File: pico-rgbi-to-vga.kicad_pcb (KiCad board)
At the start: 2 copper layers, 68.8 x 59 mm, 25 parts, among them J1 SDS-80J, J2 DB15_Female_HighDensity, J3 USB-B1HSB6, SW1 SW_Push, SW2 Intensity Select, U1 Pico

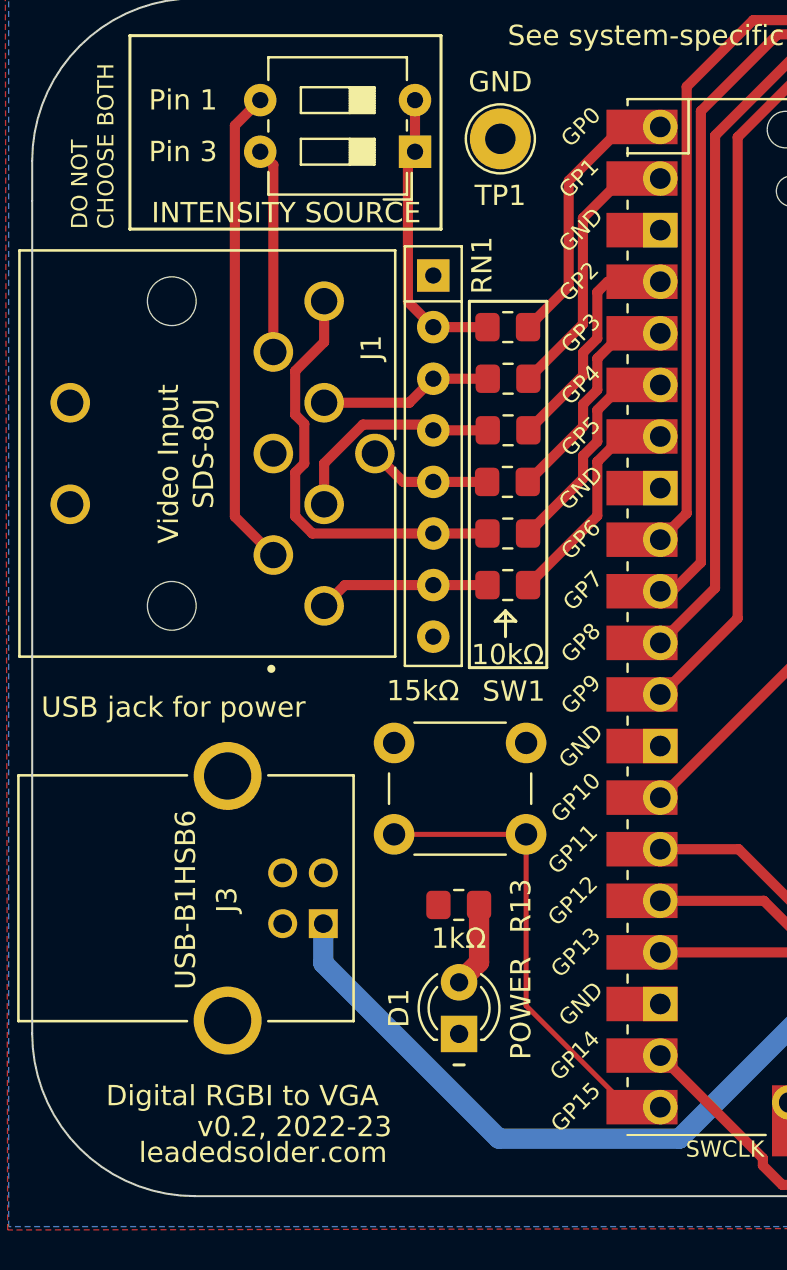
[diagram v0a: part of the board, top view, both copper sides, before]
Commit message: Fix boneheaded pinout mixup
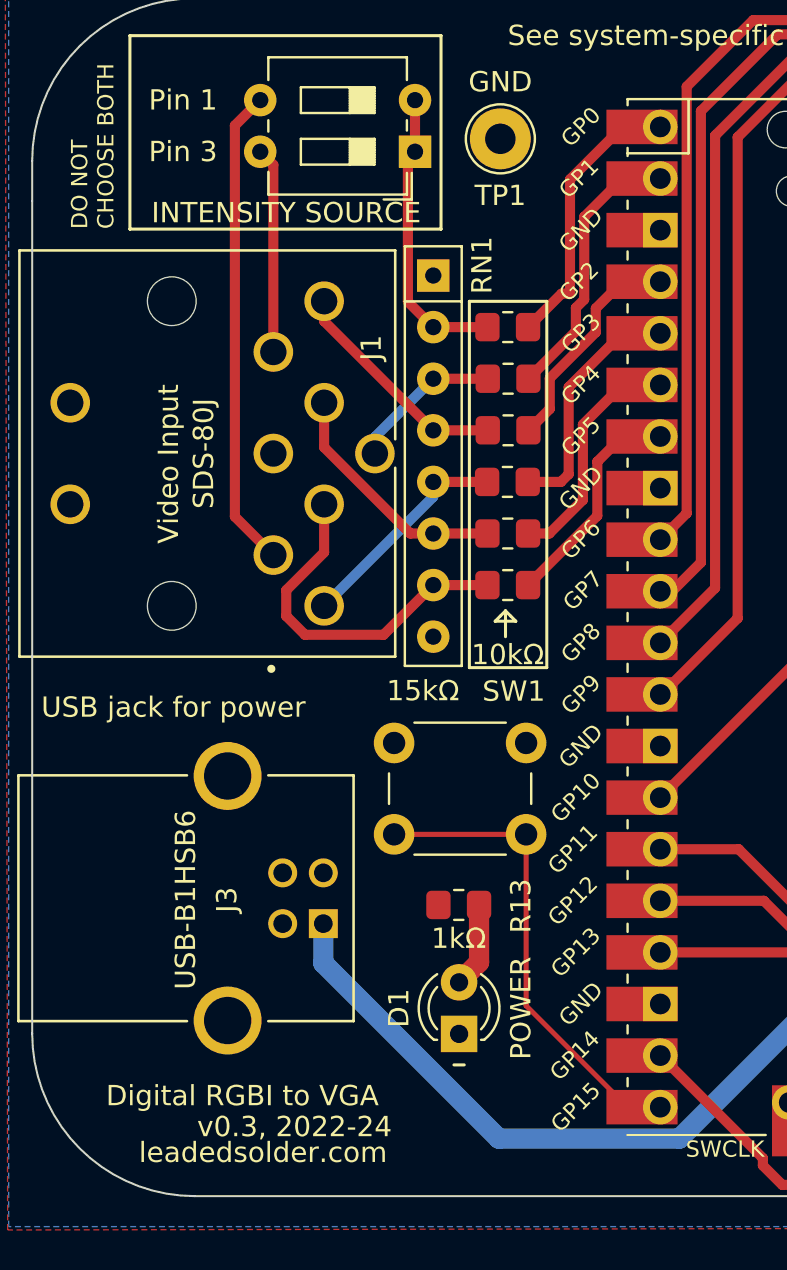
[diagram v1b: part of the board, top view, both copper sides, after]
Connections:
- R1 pad 2: /RED_IN -> /HSYNC_IN
- R2 pad 2: /GREEN_IN -> /VSYNC_IN
- R3 pad 2: /BLUE_IN -> /RED_IN
- R4 pad 2: /HSYNC_IN -> /GREEN_IN
- R5 pad 2: /VSYNC_IN -> /BLUE_IN
- RN1 pad 3: /VSYNC_IN -> /BLUE_IN
- RN1 pad 4: /HSYNC_IN -> /GREEN_IN
- RN1 pad 5: /BLUE_IN -> /RED_IN
- RN1 pad 6: /GREEN_IN -> /VSYNC_IN
- RN1 pad 7: /RED_IN -> /HSYNC_IN
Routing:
- net /GREEN_IN: track 21.4 -> 11.3 mm
- net /HSYNC_IN: track 11.0 -> 17.6 mm
- net /VSYNC_IN: track 8.55 -> 12.0 mm
- net /RED_IN: track 8.46 -> 11.0 mm
- net /BLUE_IN: track 6.10 -> 7.56 mm
- net /RED_3v3: track 11.1 -> 12.1 mm
- net /VSYNC_3v3: track 11.1 -> 11.7 mm
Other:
- board text added: "B"
- board text added: "G"
- board text added: "Hs"
- board text added: "I"
- board text added: "R"
- board text added: "Vs"
- board text added: "v0.3, 2022-24"
- board text removed: "v0.2, 2022-23"

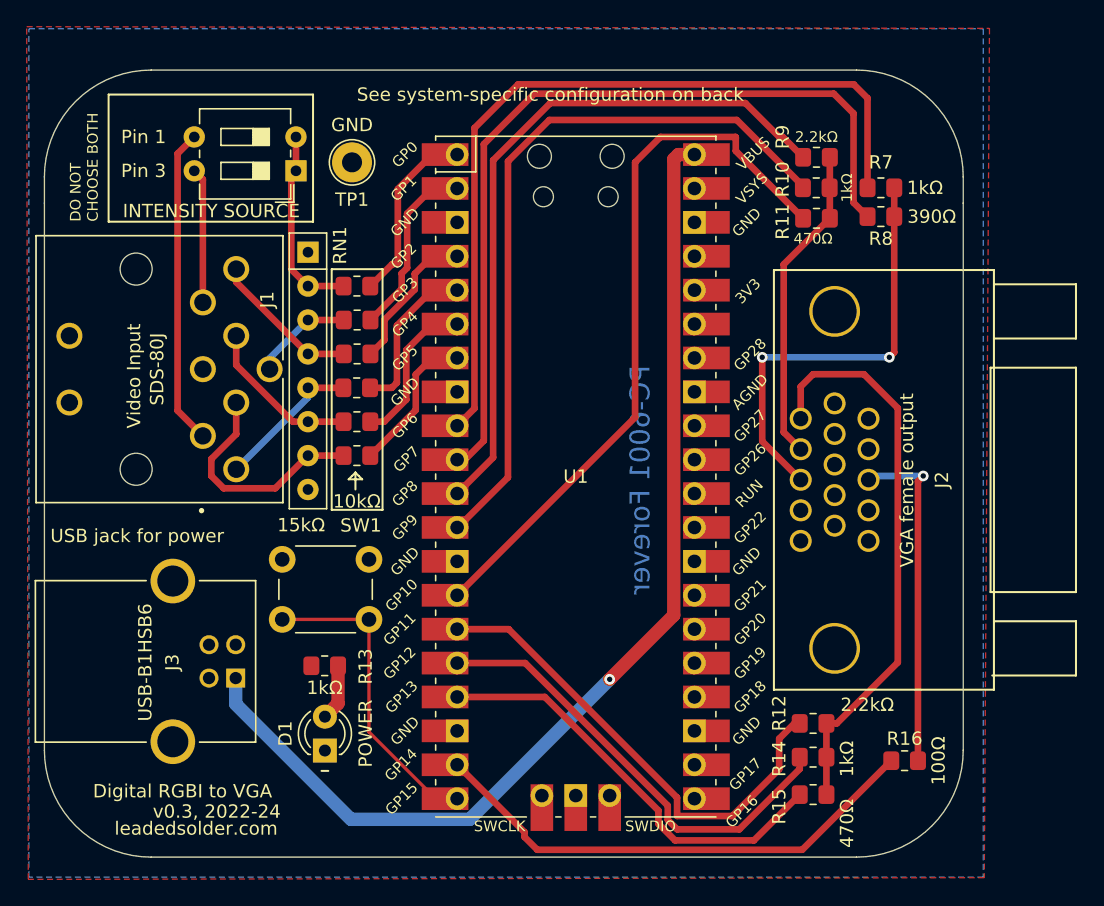
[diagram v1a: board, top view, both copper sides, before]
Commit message: V0.3 prep, adding logic analyzer lines
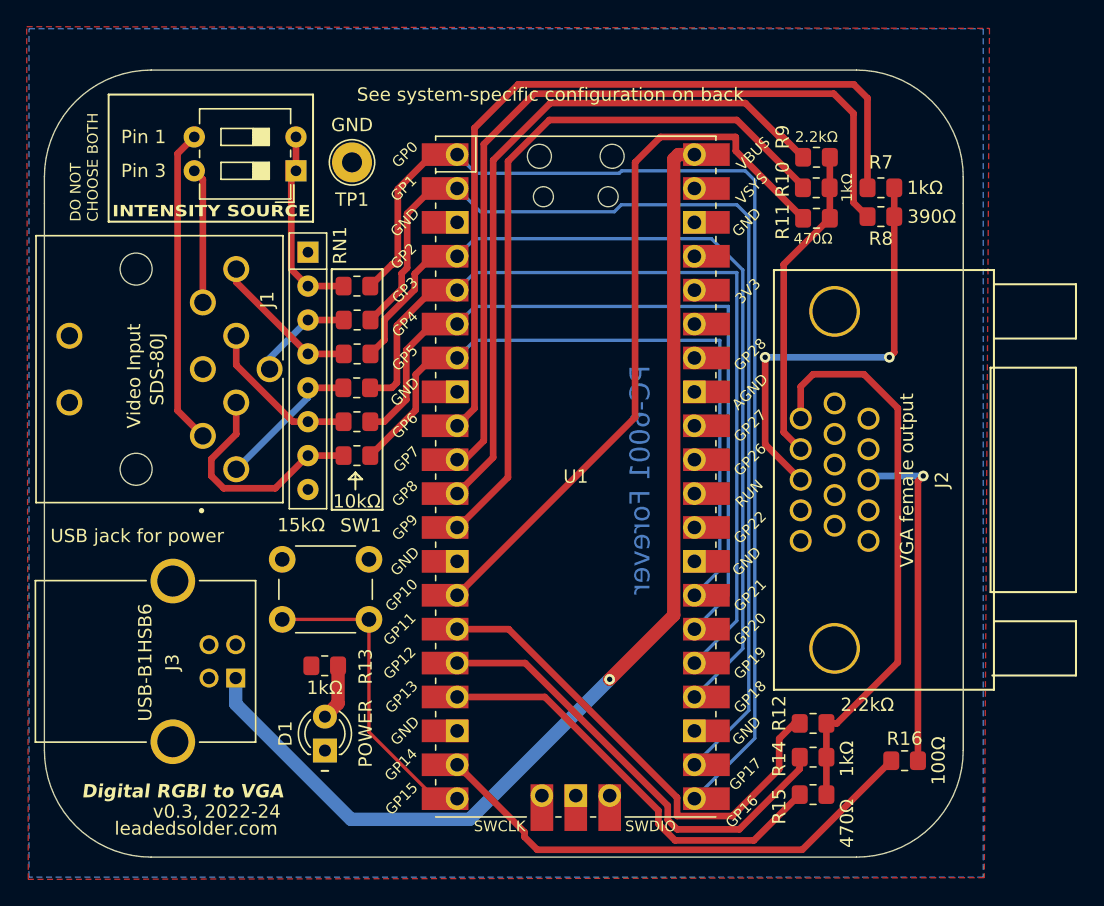
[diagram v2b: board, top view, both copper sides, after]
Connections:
- U1 pad 21: unconnected-(U1-GPIO16-Pad21) -> /INTENS_3v3
- U1 pad 22: unconnected-(U1-GPIO17-Pad22) -> /BLUE_3v3
- U1 pad 24: unconnected-(U1-GPIO18-Pad24) -> /GREEN_3v3
- U1 pad 25: unconnected-(U1-GPIO19-Pad25) -> /RED_3v3
- U1 pad 26: unconnected-(U1-GPIO20-Pad26) -> /VSYNC_3v3
- U1 pad 27: unconnected-(U1-GPIO21-Pad27) -> /HSYNC_3v3
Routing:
- net /INTENS_3v3: track 13.9 -> 85.3 mm
- net /BLUE_3v3: track 13.6 -> 79.6 mm
- net /GREEN_3v3: track 11.1 -> 67.5 mm
- net /RED_3v3: track 12.1 -> 64.1 mm
- net /VSYNC_3v3: track 11.7 -> 57.8 mm
- net /HSYNC_3v3: track 11.1 -> 51.2 mm
